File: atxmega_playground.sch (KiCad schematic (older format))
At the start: 32 parts

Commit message: Add HI-3110 CAN Transceiver
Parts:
- added D? (x4): LED, symbol LED
- added R?: 120, symbol R
- added R? (x4): 330, symbol R
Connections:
- net labels added: +5V, CANH, CANL, CAN_INT, CAN_MISO, CAN_MOSI, CAN_SCK, ~CAN_CS
- wire segments 63 -> 103
- no-connect marks 10 -> 15
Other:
- note added: "CAN Transciever"
- moved on the sheet: U?

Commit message: Add USB and Current Sense
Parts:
- removed P?: USB_B, symbol USB_B
- removed U?: MPXH6101A, symbol MPXH6101A
- added C?: C, symbol C
- added D? (x3): LED, symbol LED
- added L?: Ferrite_Bead, symbol Ferrite_Bead
- added P?: USB_OTG, symbol USB_OTG
- added Q? (x3): NMOS, cuauv:SOT-23-3, symbol NMOS
- added R?: 330, symbol R
- added R?: 620, symbol R
- added R?: 1k, symbol R
- added R?: 1, symbol R
- added U?: SN65220, symbol SN65220
- added U?: INA139, symbol INA139
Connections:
- net labels added: CURR_SENSE, PD_1, PD_2, PD_3, USB_D+, USB_D-
- wire segments 103 -> 145
- no-connect marks 15 -> 17
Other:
- note added: "CAN Transceiver"
- note added: "Current"
- note added: "Sense"
- note added: "USB"
- note added: "max 600mA"
- note removed: "CAN Transciever"
- moved on the sheet: C?, Y?

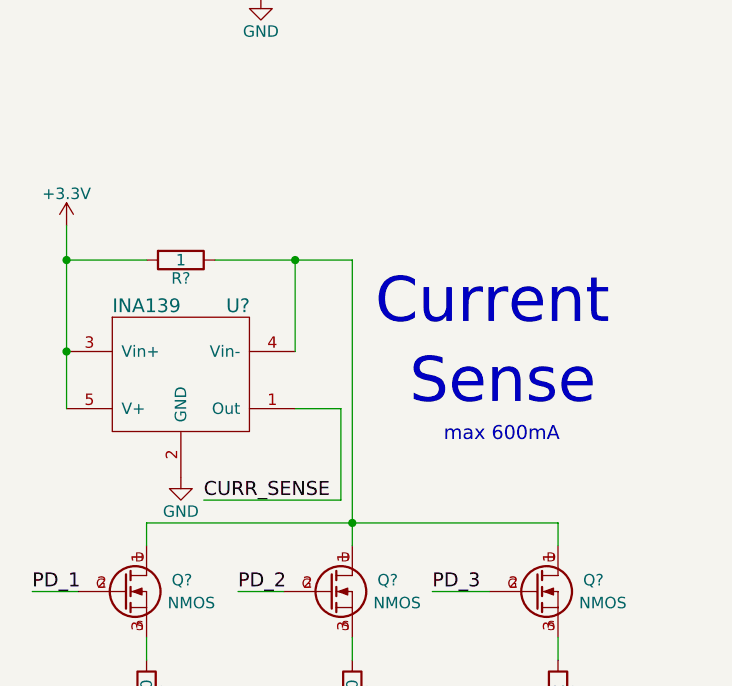
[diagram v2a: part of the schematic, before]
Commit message: Fix current sense voltage calculations
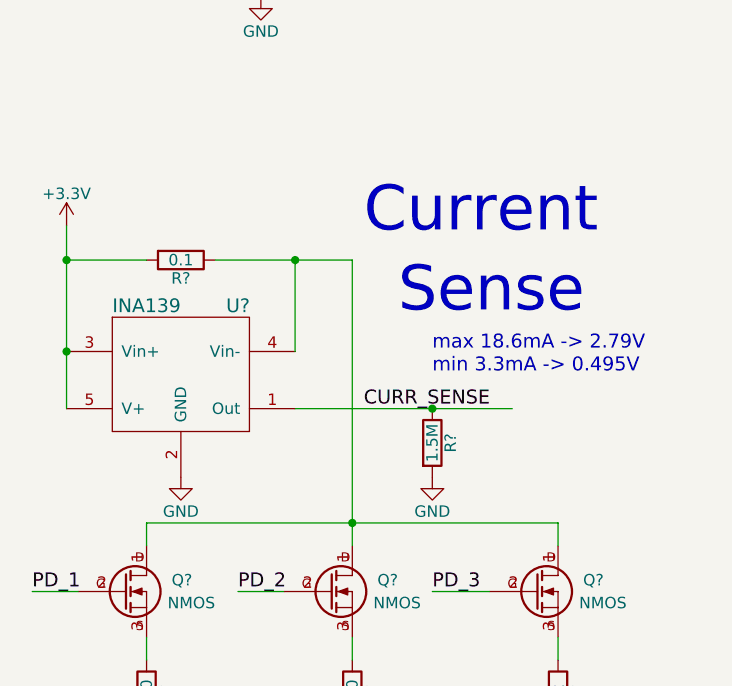
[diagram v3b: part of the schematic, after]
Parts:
- added R?: 1.5M, symbol R
- R?: value 1 -> 0.1
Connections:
- wire segments 145 -> 143
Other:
- note added: "max 18.6mA -> 2.79V"
- note added: "min 3.3mA -> 0.495V"
- note removed: "max 600mA"
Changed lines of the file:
@@
 P 16250 3850
 F 0 "R?" V 16330 3850 50  0000 C CNN
-F 1 "1" V 16250 3850 50  0000 C CNN
+F 1 "0.1" V 16250 3850 50  0000 C CNN
 F 2 "" V 16180 3850 50  0000 C CNN
 F 3 "" H 16250 3850 50  0000 C CNN
@@
 $EndComp
 Wire Wire Line
-	16750 4500 16950 4500
-Text Label 16350 4900 0    61   ~ 0
+	16750 4500 17700 4500
+Text Label 17050 4500 0    61   ~ 0
 CURR_SENSE
-Wire Wire Line
-	16950 4500 16950 4900
-Wire Wire Line
-	16950 4900 16350 4900
-Text Notes 17100 4150 0    197  ~ 0
+Text Notes 17050 3750 0    197  ~ 0
 Current
-Text Notes 17250 4500 0    197  ~ 0
+Text Notes 17200 4100 0    197  ~ 0
 Sense
 Wire Wire Line
@@
 Text Label 6400 2500 0    61   ~ 0
 CURR_SENSE
-Text Notes 17400 4650 0    61   ~ 0
-max 600mA
+Text Notes 17350 4250 0    61   ~ 0
+max 18.6mA -> 2.79V
 Wire Wire Line
 	4550 3800 4150 3800
@@
 Text Label 4150 4000 0    61   ~ 0
 PD_3
+$Comp
+L R R?
+U 1 1 5872AE32
+P 17350 4650
+F 0 "R?" V 17430 4650 50  0000 C CNN
+F 1 "1.5M" V 17350 4650 50  0000 C CNN
+F 2 "" V 17280 4650 50  0000 C CNN
+F 3 "" H 17350 4650 50  0000 C CNN
+	1    17350 4650
+	1    0    0    -1
+$EndComp
+Connection ~ 17350 4500
+$Comp
+L GND #PWR?
+U 1 1 5872AEC1
+P 17350 4800
+F 0 "#PWR?" H 17350 4550 50  0001 C CNN
+F 1 "GND" H 17350 4650 50  0000 C CNN
+F 2 "" H 17350 4800 50  0000 C CNN
+F 3 "" H 17350 4800 50  0000 C CNN
+	1    17350 4800
+	1    0    0    -1
+$EndComp
+Text Notes 17350 4350 0    61   ~ 0
+min 3.3mA -> 0.495V
 $EndSCHEMATC

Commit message: Add 74HC595 shift register and LEDs
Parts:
- removed AFF?: 7SEGMENTS, symbol 7SEGMENTS
- added D? (x8): LED, symbol LED
- added R? (x8): R, symbol R
- added R?: 10k, symbol R_Small
- added U?: 74HC595_F, symbol 74HC595_F
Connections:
- net labels added: LS_RCLK, LS_RSCLK, LS_SER, LS_SRCLK
- wire segments 143 -> 203
- no-connect marks 17 -> 18
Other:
- note added: "Shift Register"
- note added: "TODO: Change to switches?"
- moved on the sheet: AFF?

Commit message: Drive 2 7-seg displays via shift registers, add flash memory
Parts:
- removed C?: C, symbol C
- removed D? (x8): LED, symbol LED
- removed R?: R, symbol R
- removed U?: LM35, symbol LM35
- removed U?: SST25LF020A, symbol SST25LF020A
- added AFF?: 7SEGMENTS, symbol 7SEGMENTS
- added C?: C, symbol C
- added C?: 0.47uF, symbol C
- added C?: 33uF, symbol CP
- added D?: D_Zener, symbol D_Zener
- added D?: D_Schottky, symbol D_Schottky
- added F?: Fuse, symbol Fuse
- added Q?: PMOS, cuauv:SOT-23-3, symbol PMOS
- added R?: 10k, symbol R_Small
- added R? (x7): R, symbol R
- added TP?: 5V Input, symbol TEST
- added U?: AT25SF041, symbol AT25SF041
- added U?: NCP346, symbol NCP346
- added U?: 74HC595_F, symbol 74HC595_F
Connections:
- net labels added: SPIC_MISO, SPIC_MOSI, SPIC_SCK, SR2_SER, SR_RCLK, SR_RSCLK, SR_SER, SR_SRCLK, ~FLASH_CS
- net labels removed: CAN_MISO, CAN_MOSI, CAN_SCK, LS_RCLK, LS_RSCLK, LS_SER, LS_SRCLK
- wire segments 203 -> 283
- no-connect marks 18 -> 20
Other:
- note added: "7 Segment Displays"
- note added: "Flash"
- note added: "Management"
- note added: "Power"
- note added: "TODO: Change to switches"
- note removed: "Shift Register"
- moved on the sheet: AFF?, U?

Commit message: Add a few i2c sensors, power management circuitry, and digital RGB LEDs
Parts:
- added C?: 0.1uF, symbol C
- added C?: 0.22uF, symbol C
- added R? (x2): R, symbol R
- added U?: LM75BD, symbol LM75BD
- added U?: HIH9131, symbol HIH9131
- added U? (x4): WS2812B, symbol WS2812B
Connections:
- net labels added: LED_DIN_5V, SCL, SDA
- wire segments 283 -> 336
- no-connect marks 20 -> 24
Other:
- note added: "Humidity"
- note added: "RGB LEDs"
- note added: "Sensors"
- note added: "Temperature"
- moved on the sheet: AFF?, R?, U?

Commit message: Fill out MCU pins, add LEDs, (and digital pot maybe?)
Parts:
- added U?: PI4ULS5V201, symbol PI4ULS5V201
- added U?: AD5280, symbol AD5280
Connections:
- net labels added: ADC1, ADC2, ADC3, GPIO1, GPIO2, GPIO3, GPIO4, GPIO5, GPIO6, GPIO7, LED1, LED2, LED3, LED_DIN_3.3V
- wire segments 336 -> 370
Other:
- note added: "Ideas"
- note added: "LEDs"
- moved on the sheet: C?, D?, R?, U?

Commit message: Add breakout connectors
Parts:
- added P? (x2): CONN_01X02, symbol CONN_01X02
- added P? (x2): CONN_01X04, symbol CONN_01X04
- added P?: CONN_01X03, symbol CONN_01X03
- added P?: CONN_01X08, symbol CONN_01X08
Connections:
- wire segments 370 -> 399
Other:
- note added: "Connectors"
- moved on the sheet: S?
